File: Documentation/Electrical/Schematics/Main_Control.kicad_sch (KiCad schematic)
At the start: 6 parts

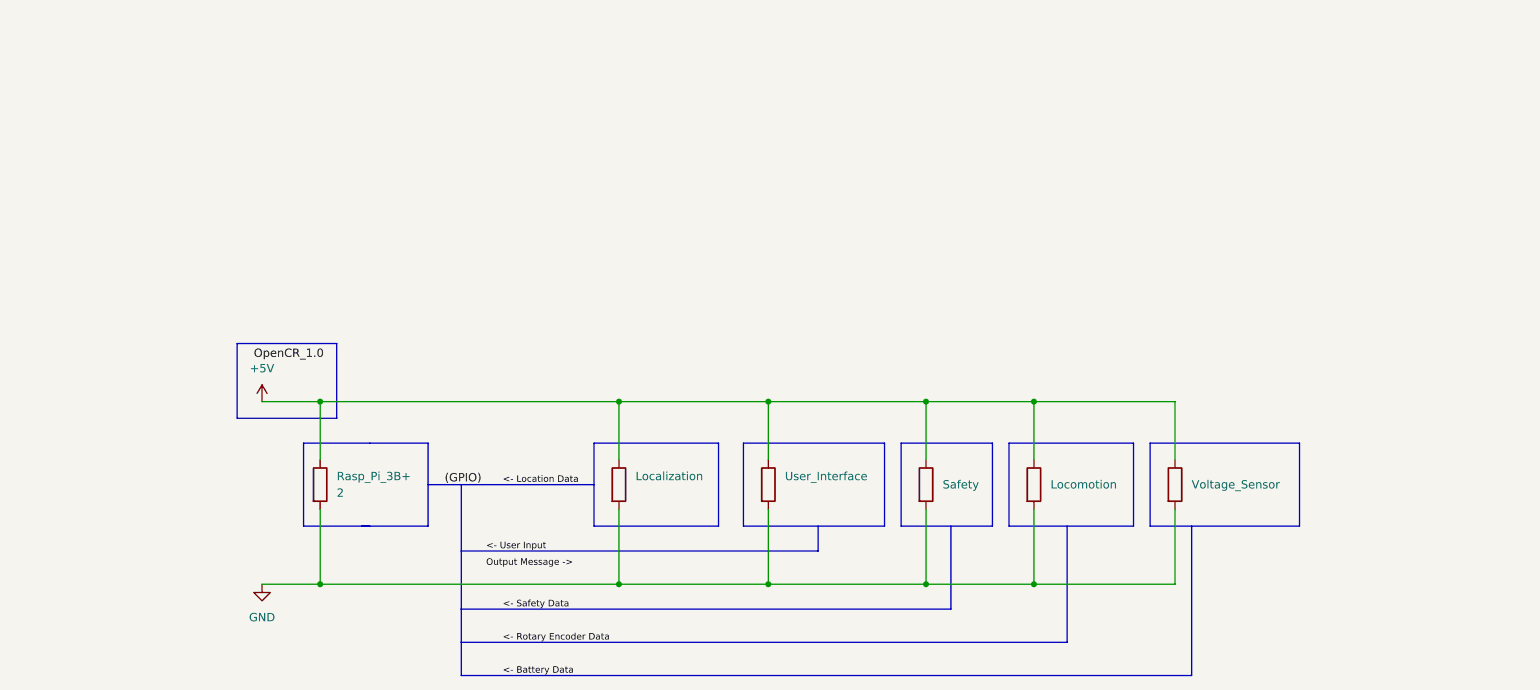
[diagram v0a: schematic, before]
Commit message: Updated Main control schematic
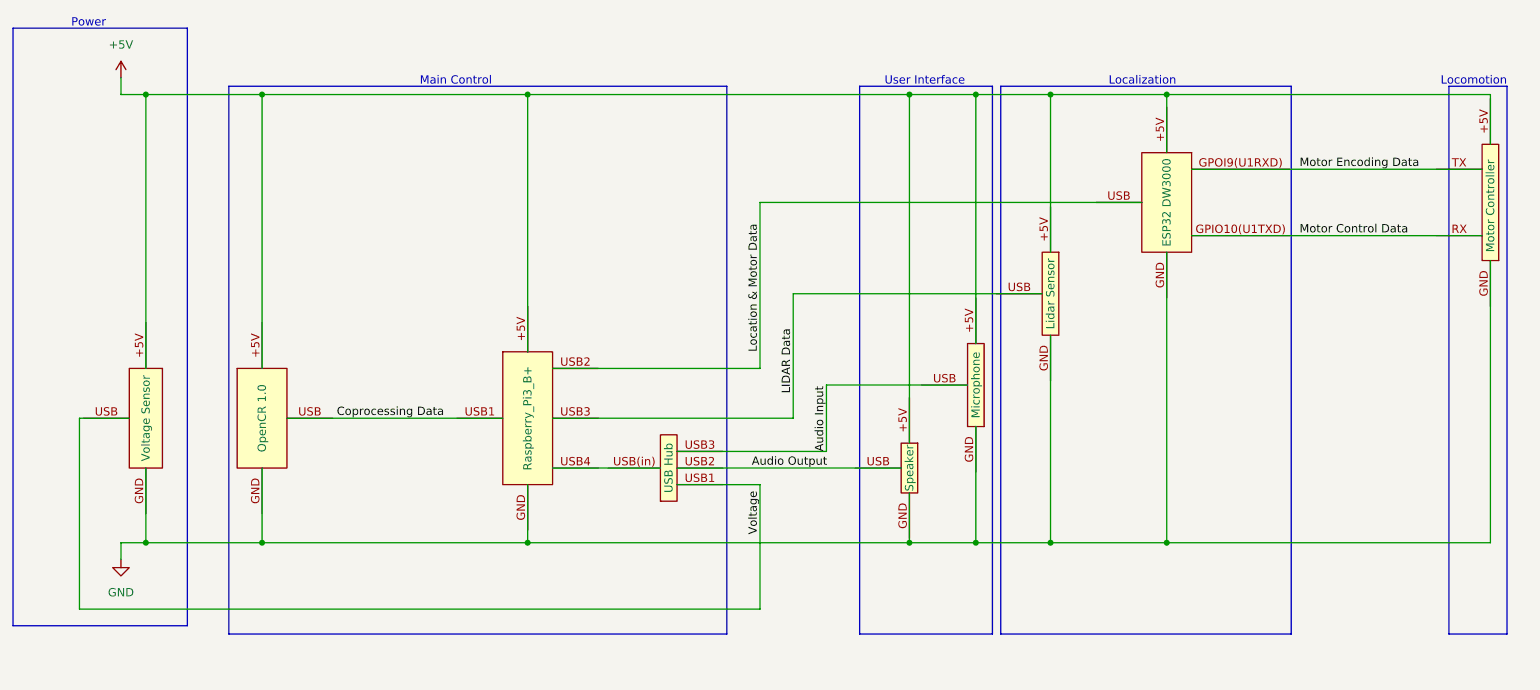
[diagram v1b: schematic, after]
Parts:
- removed Localization: 3.273, symbol Device:R
- removed Locomotion, Safety, User_Interface, Voltage_Sensor: R, symbol Device:R
- removed Rasp_Pi_3B+: 2, symbol Device:R
- added U?: Raspberry_Pi3_B+, symbol Main_Control_Components:Raspberry_Pi3_B+
- added U?: USB Hub, symbol Main_Control_Components:USB_Hub
- added U?: Motor Controller, symbol Main_Control_Components:Motor_Controller
- added U?: Speaker, symbol Main_Control_Components:Speaker
- added U?: OpenCR 1.0, symbol Main_Control_Components:OpenCR_1.0
- added U?: Voltage Sensor, symbol Main_Control_Components:Voltage_Sensor
- added U?: Microphone, symbol Main_Control_Components:Microphone
- added U?: Lidar Sensor, symbol Main_Control_Components:Lidar_Sensor
- added U?: ESP32 DW3000, symbol Main_Control_Components:ESP32 DW3000
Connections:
- net +5V: now also U?.+5V, U?.+5V, U?.+5V, U?.+5V, U?.+5V, U?.+5V, U?.+5V, U?.+5V
- net GND: now also U?.GND, U?.GND, U?.GND, U?.GND, U?.GND, U?.GND, U?.GND, U?.GND
- new net: U?.USB(in), U?.USB4
- new net Audio Input: U?.USB, U?.USB3
- new net Audio Output: U?.USB, U?.USB2
- new net Coprocessing Data: U?.USB, U?.USB1
- new net LIDAR Data: U?.USB, U?.USB3
- new net Location & Motor Data: U?.USB, U?.USB2
- new net Motor Control Data: U?.GPIO10(U1TXD), U?.RX
- new net Motor Encoding Data: U?.GPOI9(U1RXD), U?.TX
- new net Voltage: U?.USB, U?.USB1
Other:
- note added: "Localization"
- note added: "Locomotion"
- note added: "Main Control"
- note added: "Power"
- note added: "User Interface"
